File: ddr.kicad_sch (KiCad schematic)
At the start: 28 parts, among them U1 MX6UL-VM, U3 MT41K256M16

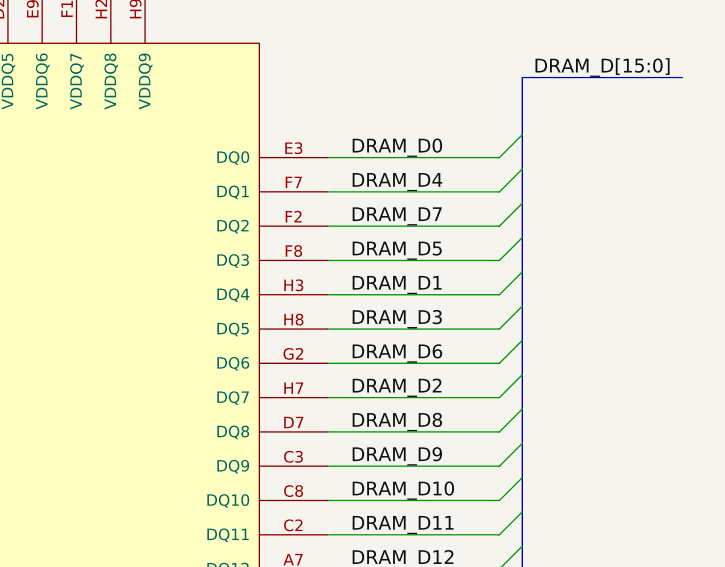
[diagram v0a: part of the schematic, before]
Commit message: more ddr routing, add more connectors
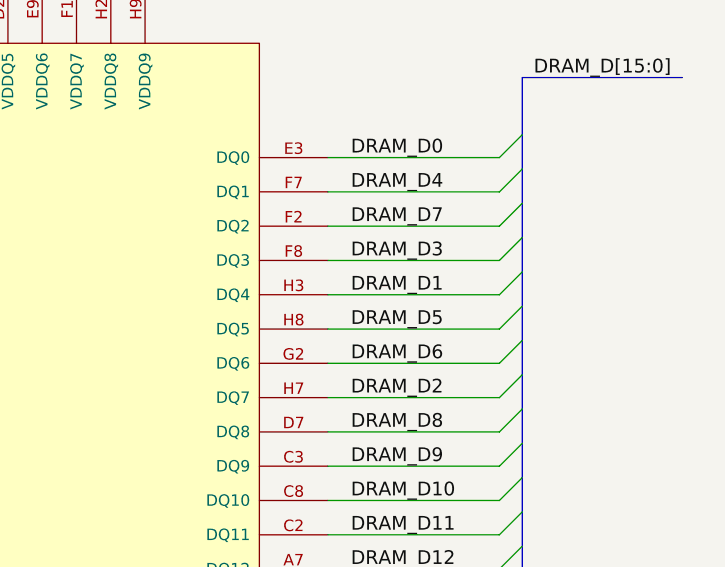
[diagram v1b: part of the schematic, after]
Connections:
- net DRAM_D3: now also U3.F8 (DQ3); no longer U3.H8 (DQ5)
- net DRAM_D5: now also U3.H8 (DQ5); no longer U3.F8 (DQ3)

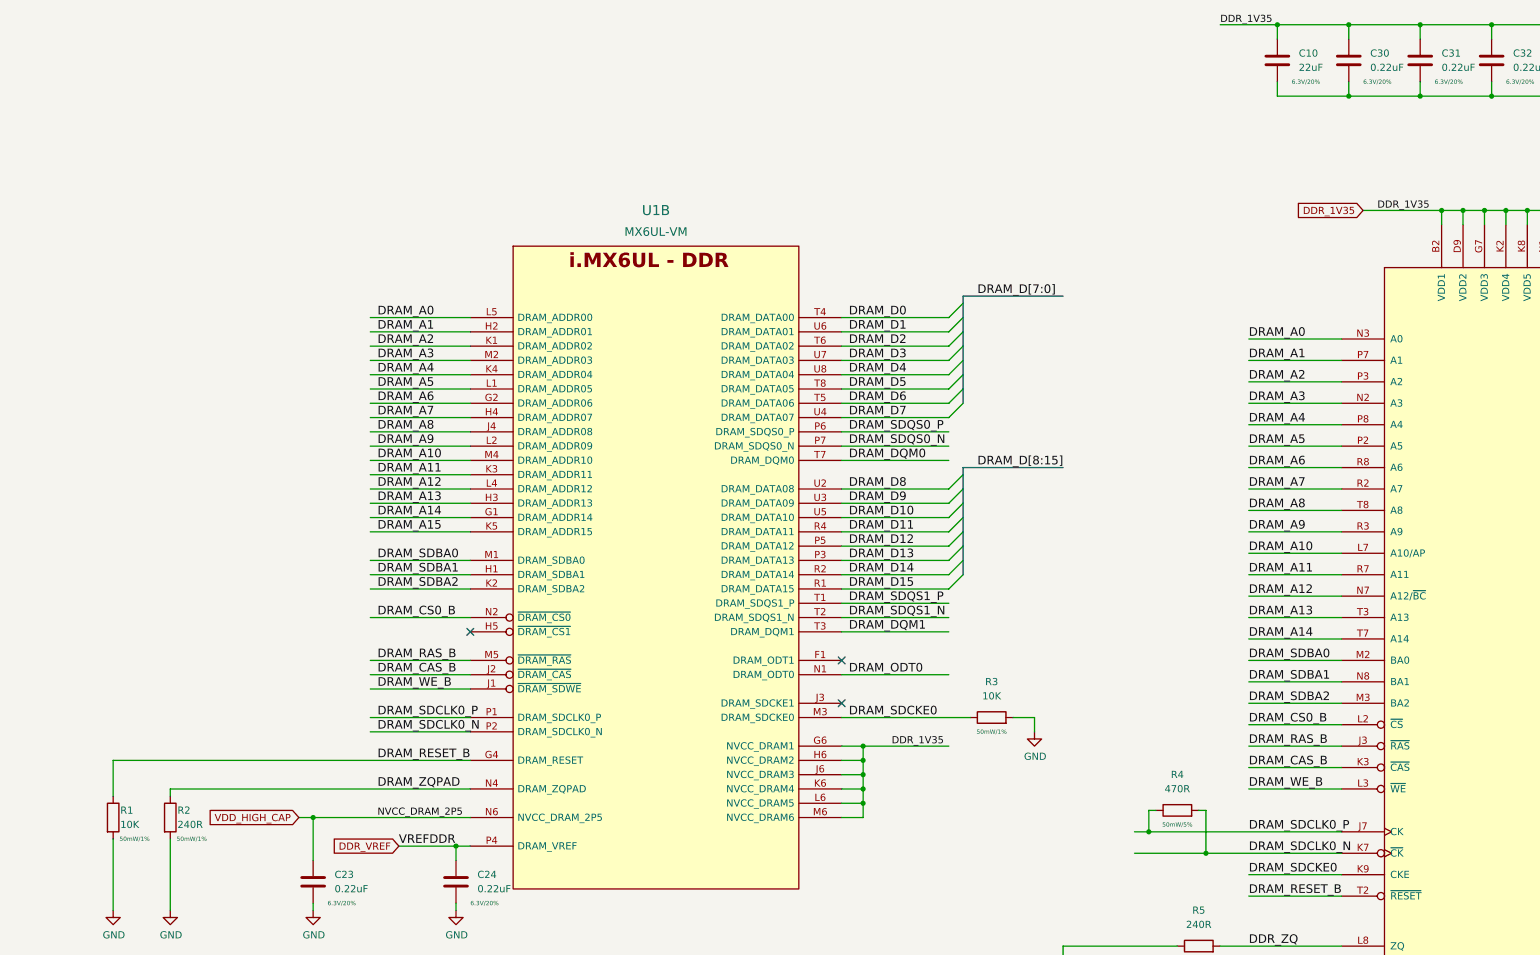
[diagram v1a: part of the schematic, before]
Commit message: start moving to hierarchal labels, add emmc
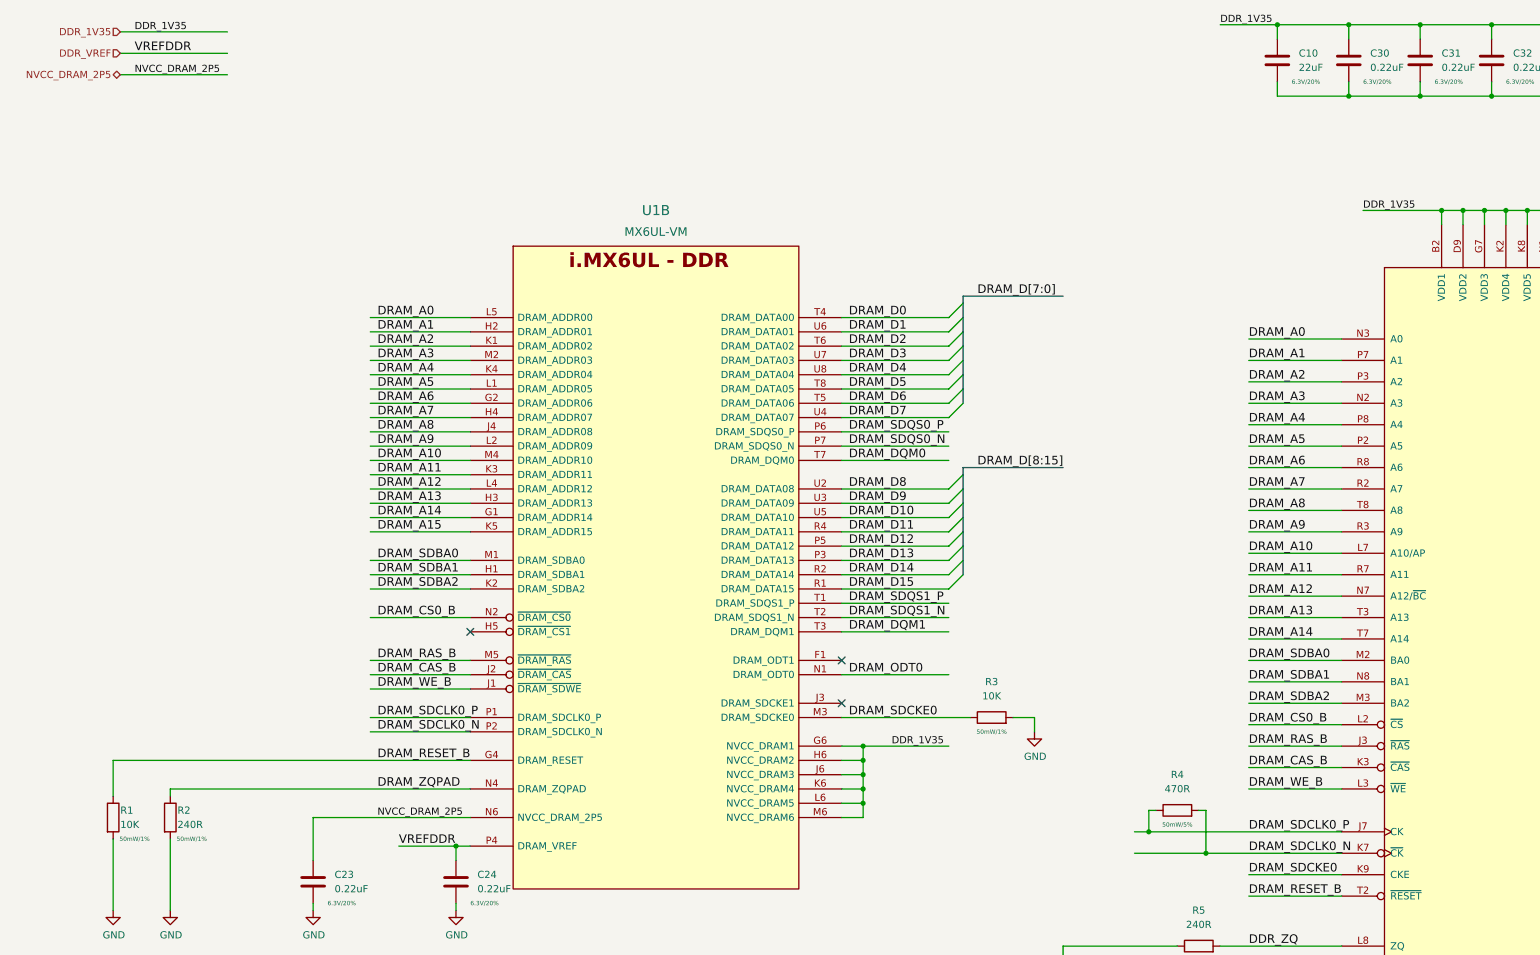
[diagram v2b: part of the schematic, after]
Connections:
- net VDD_HIGH_CAP renamed NVCC_DRAM_2P5
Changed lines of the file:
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@@
   (junction (at 335.28 232.41) (diameter 0) (color 0 0 0 0)
-  )
-  (junction (at 68.58 163.83) (diameter 0) (color 0 0 0 0)
   )
   (junction (at 123.19 208.28) (diameter 0) (color 0 0 0 0)
@@
     (stroke (width 0) (type default) (color 0 0 0 0))
   )
-  (wire (pts (xy 66.04 163.83) (xy 68.58 163.83))
-    (stroke (width 0) (type default) (color 0 0 0 0))
-  )
   (wire (pts (xy 234.95 78.74) (xy 251.46 78.74))
     (stroke (width 0) (type default) (color 0 0 0 0))
@@
     (stroke (width 0) (type default) (color 0 0 0 0))
   )
+  (wire (pts (xy 34.29 27.94) (xy 53.34 27.94))
+    (stroke (width 0) (type default) (color 0 0 0 0))
+  )
   (wire (pts (xy 148.59 220.98) (xy 148.59 218.44))
     (stroke (width 0) (type default) (color 0 0 0 0))
@@
     (stroke (width 0) (type default) (color 0 0 0 0))
   )
+  (wire (pts (xy 34.29 31.75) (xy 53.34 31.75))
+    (stroke (width 0) (type default) (color 0 0 0 0))
+  )
   (bus (pts (xy 381 95.25) (xy 381 99.06))
     (stroke (width 0) (type default) (color 0 0 0 0))
@@
   )
   (wire (pts (xy 166.37 158.75) (xy 162.56 158.75))
+    (stroke (width 0) (type default) (color 0 0 0 0))
+  )
+  (wire (pts (xy 34.29 24.13) (xy 53.34 24.13))
     (stroke (width 0) (type default) (color 0 0 0 0))
   )
@@
     (effects (font (size 1.524 1.524)) (justify left bottom))
   )
+  (label "VREFDDR" (at 36.83 27.94 0)
+    (effects (font (size 1.524 1.524)) (justify left bottom))
+  )
   (label "DRAM_A10" (at 80.01 100.33 0)
     (effects (font (size 1.524 1.524)) (justify left bottom))
@@
     (effects (font (size 1.524 1.524)) (justify left bottom))
   )
+  (label "NVCC_DRAM_2P5" (at 36.83 31.75 0)
+    (effects (font (size 1.27 1.27)) (justify left bottom))
+  )
   (label "DRAM_SDCLK0_N" (at 80.01 148.59 0)
     (effects (font (size 1.524 1.524)) (justify left bottom))
@@
     (effects (font (size 1.524 1.524)) (justify left bottom))
   )
-  (label "DDR_1V35" (at 257.81 55.88 0)
+  (label "DDR_1V35" (at 255.27 55.88 0)
     (effects (font (size 1.27 1.27)) (justify left bottom))
   )
@@
     (effects (font (size 1.524 1.524)) (justify left bottom))
   )
+  (label "DDR_1V35" (at 36.83 24.13 0)
+    (effects (font (size 1.27 1.27)) (justify left bottom))
+  )
   (label "DRAM_D8" (at 163.83 105.41 0)
     (effects (font (size 1.524 1.524)) (justify left bottom))
@@
     (effects (font (size 1.524 1.524)) (justify left bottom))
   )
-  (global_label "DDR_1V35" (shape input) (at 255.27 55.88 180) (fields_autoplaced)
+  (hierarchical_label "NVCC_DRAM_2P5" (shape bidirectional) (at 34.29 31.75 180)
     (effects (font (size 1.27 1.27)) (justify right))
-    (property "Intersheet References" "${INTERSHEET_REFS}" (id 0) (at 2.54 -7.62 0)
-      (effects (font (size 1.27 1.27)) hide)
-    )
-  )
-  (global_label "VDD_HIGH_CAP" (shape input) (at 66.04 163.83 180) (fields_autoplaced)
+  )
+  (hierarchical_label "DDR_1V35" (shape input) (at 34.29 24.13 180)
     (effects (font (size 1.27 1.27)) (justify right))
-    (property "Intersheet References" "${INTERSHEET_REFS}" (id 0) (at 11.43 41.91 0)
-      (effects (font (size 1.27 1.27)) hide)
-    )
-  )
-  (global_label "DDR_VREF" (shape input) (at 83.82 168.91 180) (fields_autoplaced)
+  )
+  (hierarchical_label "DDR_VREF" (shape input) (at 34.29 27.94 180)
     (effects (font (size 1.27 1.27)) (justify right))
-    (property "Intersheet References" "${INTERSHEET_REFS}" (id 0) (at 11.43 41.91 0)
-      (effects (font (size 1.27 1.27)) hide)
-    )
   )
   (symbol (lib_id "power:GND") (at 213.36 226.06 0) (unit 1)

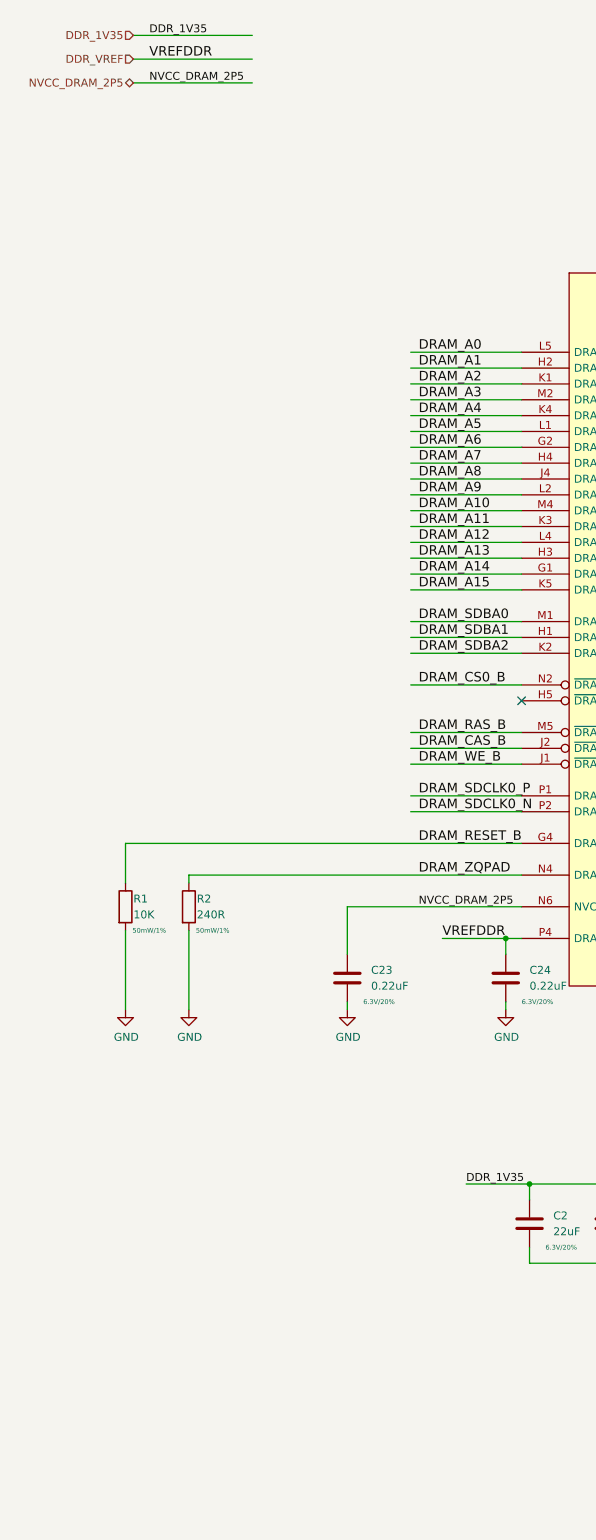
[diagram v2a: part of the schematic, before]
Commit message: move to hierarchal labels, work on power tree, add basic pcb layout
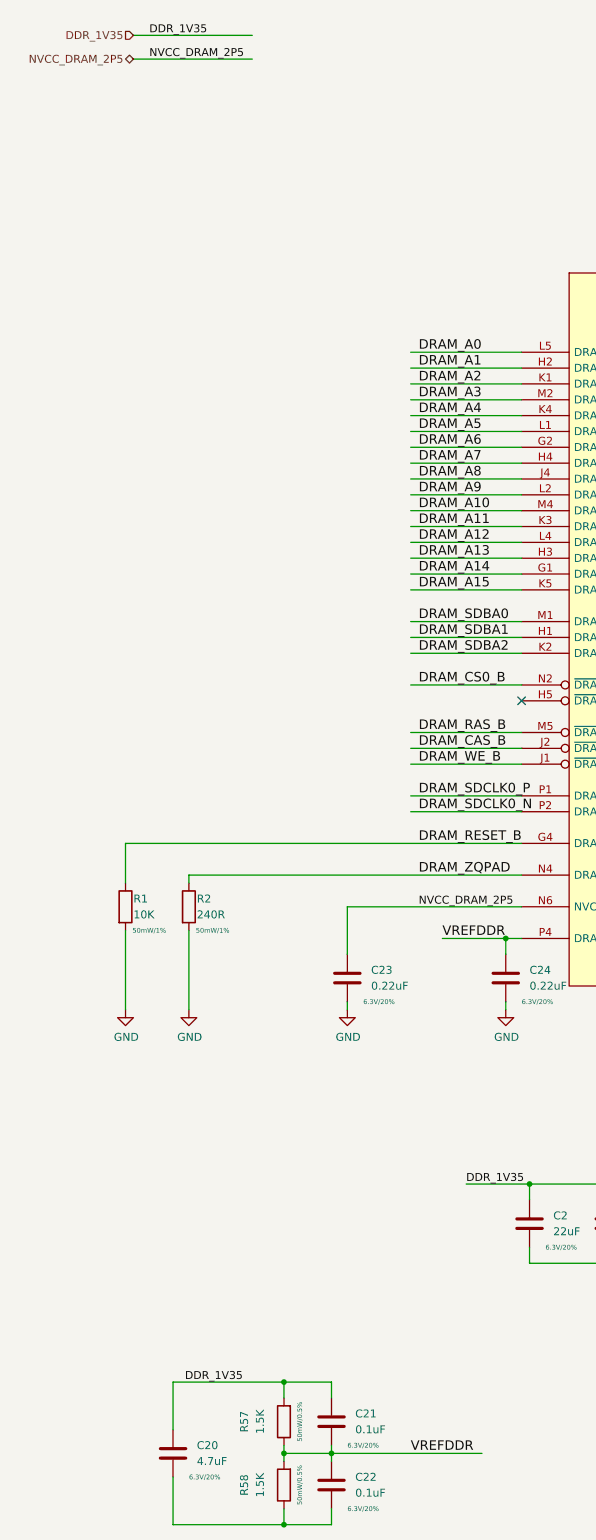
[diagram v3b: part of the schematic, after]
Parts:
- added C20: 4.7uF, Capacitor_SMD:C_0402_1005Metric, symbol Device:C
- added C21, C22: 0.1uF, Capacitor_SMD:C_0402_1005Metric, symbol Device:C
- added R57, R58: 1.5K, Resistor_SMD:R_0402_1005Metric, symbol Device:R
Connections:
- net DDR_1V35: now also C20.1, C21.1, R57.2
- net DDR_VREF renamed VREFDDR
- net VREFDDR: now also C21.2, C22.1, R57.1, R58.2
- new net: C20.2, C22.2, R58.1

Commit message: lots of routing, ddr length matching done
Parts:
- U1: footprint imx6ull-sbc:SOT1534-2 -> qsbc-zero:SOT1534-2; symbol imx6ull-sbc:MX6UL-VM -> qsbc-zero:MX6UL-VM
- U3: footprint imx6ull-sbc:MICRON-FBGA-96 -> qsbc-zero:MICRON-FBGA-96; symbol imx6ull-sbc:MT41K256M16 -> qsbc-zero:MT41K256M16
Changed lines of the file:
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@@
     (pin "1")
   )
-  (symbol (lib_id "imx6ull-sbc:MT41K256M16") (at 304.8 140.97 0) (unit 1)
+  (symbol (lib_id "qsbc-zero:MT41K256M16") (at 304.8 140.97 0) (unit 1)
     (in_bom yes) (on_board yes)
     (property "Reference" "U3" (id 0) (at 305.271 137.0662 0)
@@
       (effects (font (size 2.9972 2.9972)))
     )
-    (property "Footprint" "imx6ull-sbc:MICRON-FBGA-96" (id 2) (at 304.8 143.51 0)
+    (property "Footprint" "qsbc-zero:MICRON-FBGA-96" (id 2) (at 304.8 143.51 0)
       (effects (font (size 1.524 1.524)) hide)
     )
@@
     (pin "2")
   )
-  (symbol (lib_id "imx6ull-sbc:MX6UL-VM") (at 129.54 62.23 0) (unit 2)
+  (symbol (lib_id "qsbc-zero:MX6UL-VM") (at 129.54 62.23 0) (unit 2)
     (in_bom yes) (on_board yes) (fields_autoplaced)
     (property "Reference" "U1" (id 0) (at 129.54 55.88 0)
@@
       (effects (font (size 1.524 1.524)))
     )
-    (property "Footprint" "imx6ull-sbc:SOT1534-2" (id 2) (at 142.494 91.694 0)
+    (property "Footprint" "qsbc-zero:SOT1534-2" (id 2) (at 142.494 91.694 0)
       (effects (font (size 1.524 1.524)) hide)
     )

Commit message: more pcb work, bom work
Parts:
- added R21: 10K, Resistor_SMD:R_0402_1005Metric, symbol Device:R
- C10, C2: DigiKey_PN (none) -> 490-7611-1-ND; MPN (none) -> GRM188R60J226MEA0D
- C20: DigiKey_PN (none) -> 1276-1482-1-ND; MPN (none) -> CL05A475MP5NRNC; Rating 6.3V/20% -> 10V/20%
- C21, C22: DigiKey_PN (none) -> 490-14603-1-ND; MPN (none) -> GRM155R71E104KE14J; Rating 6.3V/20% -> 25V/20%
- C23, C24, C25, C26, C27, C28, C29, C30, C31, C32, C33, C34, C35, C36, C37, C38, C39, C4, C40: DigiKey_PN (none) -> 490-10392-1-ND; MPN (none) -> GRM033C80J224KE90D
- R1, R3: DigiKey_PN (none) -> 311-10KJRCT-ND; MPN (none) -> RC0402JR-0710KL; Rating 50mW/1% -> 50mW/5%
- R2: DigiKey_PN (none) -> 311-240LRCT-ND; MPN (none) -> RC0402FR-07240RL
- R4: footprint Capacitor_SMD:C_0201_0603Metric -> Resistor_SMD:R_0201_0603Metric; DigiKey_PN (none) -> 311-470NCT-ND; MPN (none) -> RC0201JR-07470RL
- R5: footprint Resistor_SMD:R_0402_1005Metric -> Resistor_SMD:R_0201_0603Metric; DigiKey_PN (none) -> 311-240LRCT-ND; MPN (none) -> RC0402FR-07240RL
- R57, R58: DigiKey_PN (none) -> 311-2246-1-ND; MPN (none) -> RT0402DRE071K5L
- U1: DigiKey_PN (none) -> 568-14995-ND; MPN (none) -> MCIMX6Y2DVM09AB
- U3: DigiKey_PN (none) -> 557-1792-ND; MPN (none) -> MT41K256M16TW-107:P
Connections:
- net GND: now also C20.2, C22.2, R58.1, R21.2
- net DRAM_SDCKE1: now reaches U1.F1 (DRAM_ODT1)
- net DRAM_SDCKE1: now also R21.1
- no-connect marks 7 -> 6

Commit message: add basic readme, rev 1 of pcb
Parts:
- removed C20: 4.7uF, Capacitor_SMD:C_0402_1005Metric, symbol Device:C
- removed C21, C22: 0.1uF, Capacitor_SMD:C_0402_1005Metric, symbol Device:C
- removed R57, R58: 1.5K, Resistor_SMD:R_0402_1005Metric, symbol Device:R
- C10, C2: DigiKey_PN 490-7611-1-ND -> 1276-1274-1-ND; MPN GRM188R60J226MEA0D -> CL10A226MP8NUNE; Rating 6.3V/20% -> 10V/20%
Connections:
- net VREFDDR renamed DDR_VREF

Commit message: misc rev2 fixes
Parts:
- R2, R5: DigiKey_PN 311-240LRCT-ND -> YAG2528CT-ND; MPN RC0402FR-07240RL -> RC0201FR-07240RL
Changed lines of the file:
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@@
       (effects (font (size 0.762 0.762)))
     )
-    (property "DigiKey_PN" "311-240LRCT-ND" (id 5) (at 43.18 163.83 0)
-      (effects (font (size 1.27 1.27)) hide)
-    )
-    (property "MPN" "RC0402FR-07240RL" (id 6) (at 43.18 163.83 0)
+    (property "DigiKey_PN" "YAG2528CT-ND" (id 5) (at 43.18 163.83 0)
+      (effects (font (size 1.27 1.27)) hide)
+    )
+    (property "MPN" "RC0201FR-07240RL" (id 6) (at 43.18 163.83 0)
       (effects (font (size 1.27 1.27)) hide)
     )
@@
       (effects (font (size 0.762 0.762)))
     )
-    (property "DigiKey_PN" "311-240LRCT-ND" (id 5) (at 226.06 186.69 0)
-      (effects (font (size 1.27 1.27)) hide)
-    )
-    (property "MPN" "RC0402FR-07240RL" (id 6) (at 226.06 186.69 0)
-      (effects (font (size 1.27 1.27)) hide)
-    )
+    (property "DigiKey_PN" "YAG2528CT-ND" (id 5) (at 226.06 186.69 0)
+      (effects (font (size 1.27 1.27)) hide)
+    )
+    (property "MPN" "RC0201FR-07240RL" (id 6) (at 226.06 186.69 0)
+      (effects (font (size 1.27 1.27)) hide)
+    )
